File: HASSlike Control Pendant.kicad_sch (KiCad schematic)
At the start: 279 parts, among them SW1 SW_Push, SW10 SW_Push, SW100 SW_Push, SW101 SW_Push, SW102 SW_Push, SW103 SW_Push, SW104 SW_Push, SW105 SW_Push, SW106 SW_Push, SW107 SW_Push, SW108 SW_Push, SW109 SW_Push, SW11 SW_Push, SW110 SW_Push, SW111 SW_Push, SW112 SW_Push, SW113 SW_Push, SW114 SW_Push, SW115 SW_Push, SW116 SW_Push, SW117 SW_Push, SW118 SW_Push, SW119 SW_Push, SW12 SW_Push, SW120 SW_Push, SW121 SW_Push, SW122 SW_Push, SW123 SW_Push, SW124 SW_Push, SW125 SW_Push, SW126 SW_Push, SW127 SW_Push, SW128 SW_Push, SW129 SW_Push, SW13 SW_Push, SW130 SW_Push, SW131 SW_Push, SW132 SW_Push, SW133 SW_Push, SW134 SW_Push, SW135 SW_Push, SW136 SW_Push, SW137 SW_Push, SW138 SW_Push, SW139 SW_Push, SW14 SW_Push, SW15 SW_Push, SW16 SW_Push, SW17 SW_Push, SW18 SW_Push, SW19 SW_Push, SW2 SW_Push, SW20 SW_Push, SW21 SW_Push, SW22 SW_Push, SW23 SW_Push, SW24 SW_Push, SW25 SW_Push, SW26 SW_Push, SW27 SW_Push, SW28 SW_Push, SW29 SW_Push, SW3 SW_Push, SW30 SW_Push, SW31 SW_Push, SW32 SW_Push, SW33 SW_Push, SW34 SW_Push, SW35 SW_Push, SW36 SW_Push, SW37 SW_Push, SW38 SW_Push, SW39 SW_Push, SW4 SW_Push, SW40 SW_Push, SW41 SW_Push, SW42 SW_Push, SW43 SW_Push, SW44 SW_Push, SW45 SW_Push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

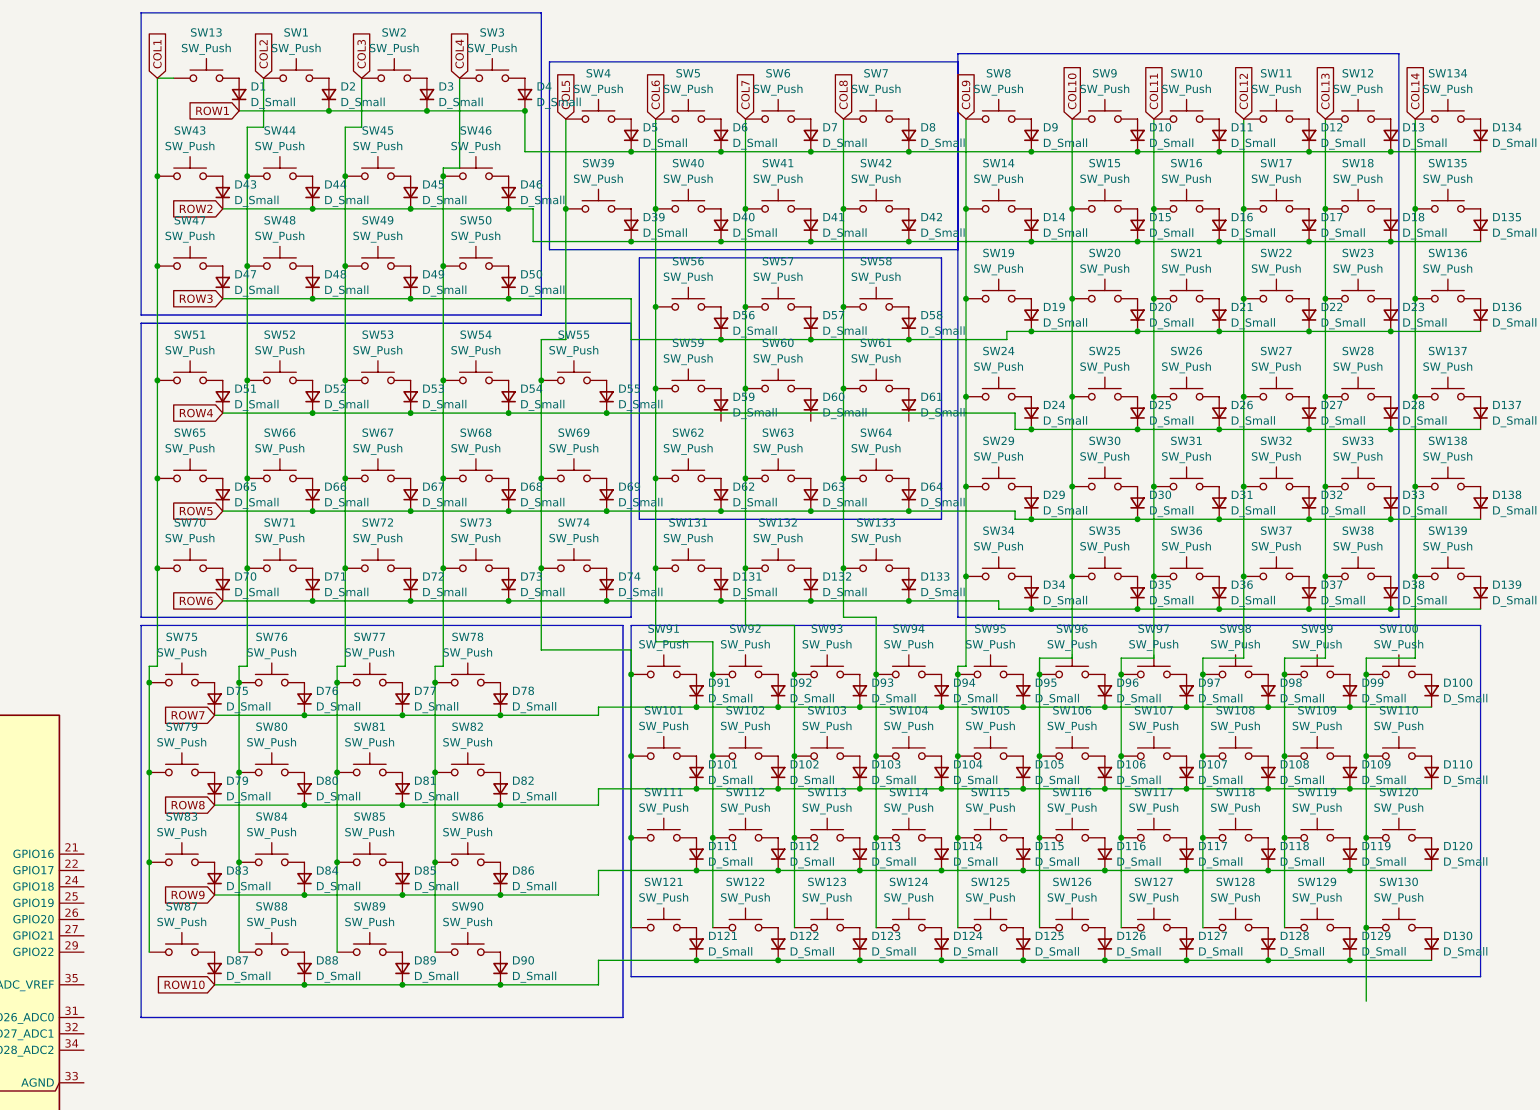
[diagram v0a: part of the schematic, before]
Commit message: start on pcb layout for monolithic implementation
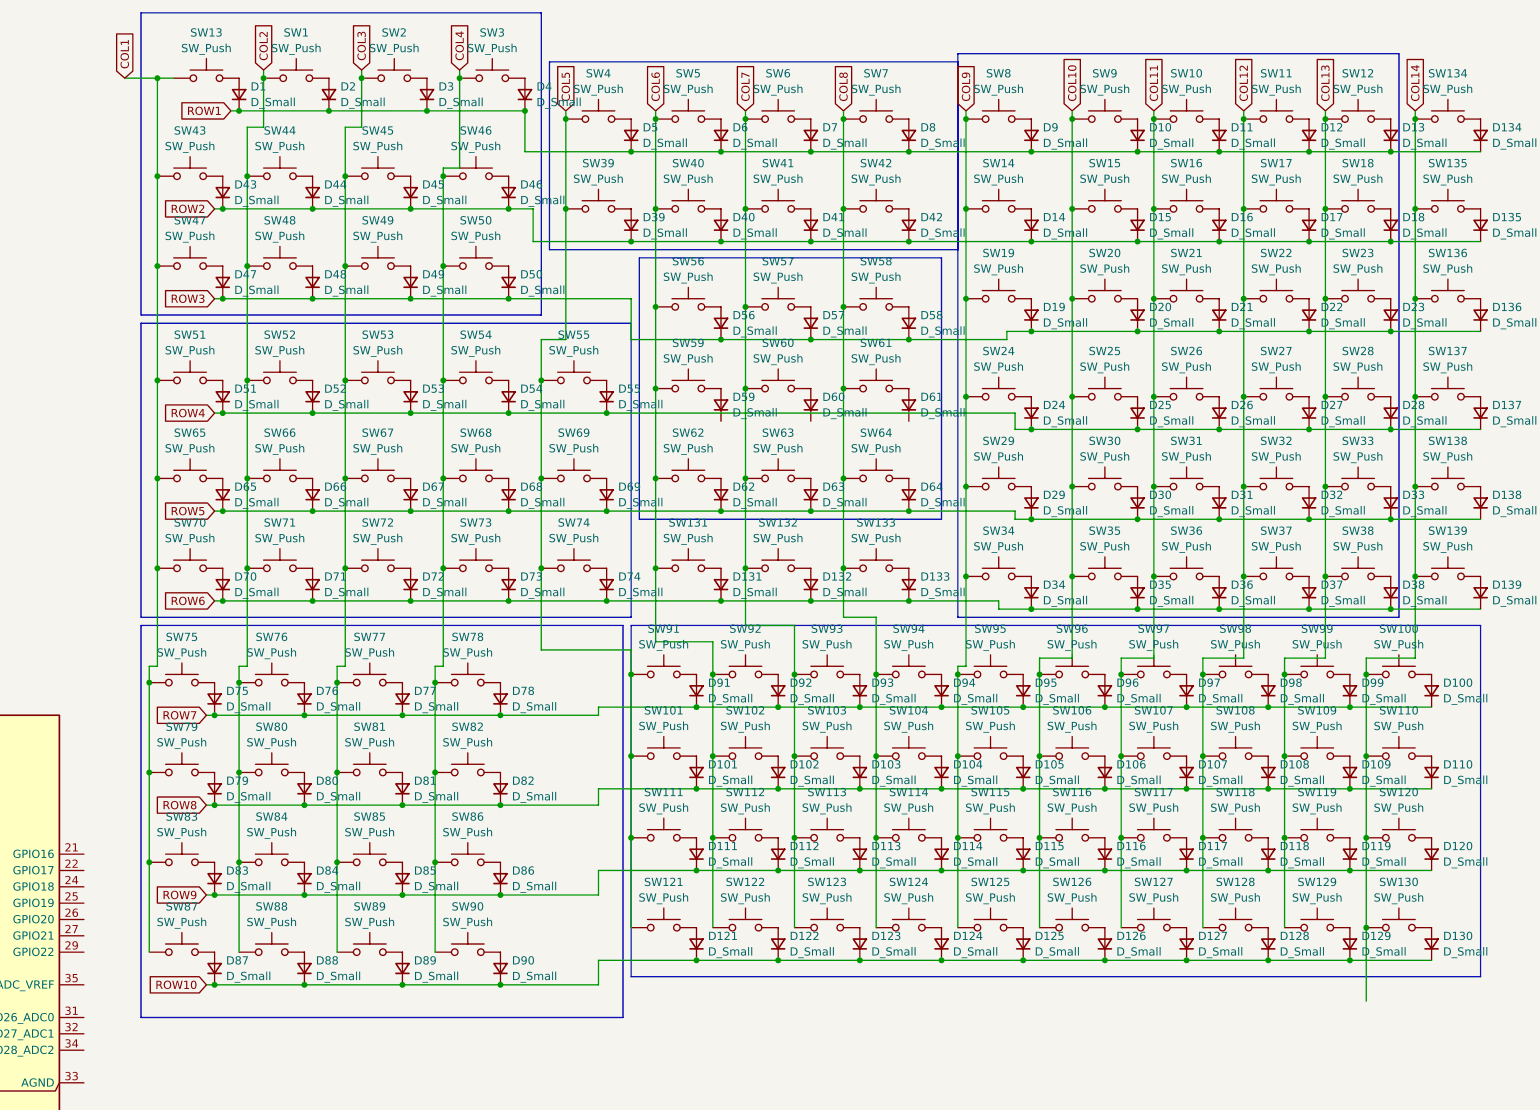
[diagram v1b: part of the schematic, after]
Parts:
- D1, D10, D100, D101, D102, D103, D104, D105, D106, D107, D108, D109, D11, D110, D111, D112, D113, D114, D115, D116, D117, D118, D119, D12, D120, D121, D122, D123, D124, D125, D126, D127, D128, D129, D13, D130, D131, D132, D133, D134, D135, D136, D137, D138, D139, D14, D15, D16, D17, D18, D19, D2, D20, D21, D22, D23, D24, D25, D26, D27, D28, D29, D3, D30, D31, D32, D33, D34, D35, D36, D37, D38, D39, D4, D40, D41, D42, D43, D44, D45, D46, D47, D48, D49, D5, D50, D51, D52, D53, D54, D55, D56, D57, D58, D59, D6, D60, D61, D62, D63, D64, D65, D66, D67, D68, D69, D7, D70, D71, D72, D73, D74, D75, D76, D77, D78, D79, D8, D80, D81, D82, D83, D84, D85, D86, D87, D88, D89, D9, D90, D91, D92, D93, D94, D95, D96, D97, D98, D99: footprint (none) -> Diode_SMD:D_SOT-23_MMDB4148_BAS21_BAT54
- SW1, SW10, SW100, SW101, SW102, SW103, SW104, SW105, SW106, SW107, SW108, SW109, SW11, SW110, SW111, SW112, SW113, SW114, SW115, SW116, SW117, SW118, SW119, SW12, SW120, SW121, SW122, SW123, SW124, SW125, SW126, SW127, SW128, SW129, SW13, SW130, SW131, SW132, SW133, SW134, SW135, SW136, SW137, SW138, SW139, SW14, SW15, SW16, SW17, SW18, SW19, SW2, SW20, SW21, SW22, SW23, SW24, SW25, SW26, SW27, SW28, SW29, SW3, SW30, SW31, SW32, SW33, SW34, SW35, SW36, SW37, SW38, SW39, SW4, SW40, SW41, SW42, SW43, SW44, SW45, SW46, SW47, SW48, SW49, SW5, SW50, SW51, SW52, SW53, SW54, SW55, SW56, SW57, SW58, SW59, SW6, SW60, SW61, SW62, SW63, SW64, SW65, SW66, SW67, SW68, SW69, SW7, SW70, SW71, SW72, SW73, SW74, SW75, SW76, SW77, SW78, SW79, SW8, SW80, SW81, SW82, SW83, SW84, SW85, SW86, SW87, SW88, SW89, SW9, SW90, SW91, SW92, SW93, SW94, SW95, SW96, SW97, SW98, SW99: footprint (none) -> PCM_Switch_Keyboard_Hybrid:SW_Hybrid_Cherry_MX_Alps_1.00u

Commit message: progress on layout for small-scale proof of concept board
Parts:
- removed D100, D101, D102, D103, D104, D105, D106, D107, D108, D109, D110, D111, D112, D113, D114, D115, D116, D117, D118, D119, D120, D121, D122, D123, D124, D125, D126, D127, D128, D129, D130, D75, D76, D77, D78, D79, D80, D81, D82, D83, D84, D85, D86, D87, D88, D89, D90, D91, D92, D93, D94, D95, D96, D97, D98, D99: D_Small, Diode_SMD:D_SOT-23_MMDB4148_BAS21_BAT54, symbol Device:D_Small
- removed SW100, SW101, SW102, SW103, SW104, SW105, SW106, SW107, SW108, SW109, SW110, SW111, SW112, SW113, SW114, SW115, SW116, SW117, SW118, SW119, SW120, SW121, SW122, SW123, SW124, SW125, SW126, SW127, SW128, SW129, SW130, SW75, SW76, SW77, SW78, SW79, SW80, SW81, SW82, SW83, SW84, SW85, SW86, SW87, SW88, SW89, SW90, SW91, SW92, SW93, SW94, SW95, SW96, SW97, SW98, SW99: SW_Push, PCM_Switch_Keyboard_Hybrid:SW_Hybrid_Cherry_MX_Alps_1.00u, symbol Switch:SW_Push
- added J2: Conn_01x04_Pin, Connector_JST:JST_SH_BM04B-SRSS-TB_1x04-1MP_P1.00mm_Vertical, symbol Connector:Conn_01x04_Pin
- A1: footprint Module:RaspberryPi_Pico_W_SMD_HandSolder -> Module:RaspberryPi_Pico_Common_Unspecified
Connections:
- net GND: now reaches A1.13 (GND), A1.18 (GND), A1.23 (GND), A1.28 (GND), A1.3 (GND), A1.38 (GND), A1.8 (GND), A1.D2 (GND)
- net GND: now also J2.1 (Pin_1)
- net VCC: now reaches A1.36 (3V3)
- net VCC: now also J2.2 (Pin_2)
- new net SCL: J2.4 (Pin_4)
- new net SDA: J2.3 (Pin_3)
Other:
- added sheet 4x4Test (4x4.kicad_sch)
- added sheet AlphanumericSection (Alphanumeric.kicad_sch)
- note added: "4x4"
